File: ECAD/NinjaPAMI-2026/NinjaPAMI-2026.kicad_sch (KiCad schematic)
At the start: 76 parts, among them J1 Con_Batt, J10 CON_EV_01, J11 Conn_01x04, J12 OLED, J13 RightMotor, J14 LeftMotor, J2 Servo, J3 Servo, J4 Sensor_RIGHT, J5 Sensor_Center, J6 Sensor_LEFT, J7 CON_EV_02, J8 CON_EV_02, J9 CON_PUMP_01, Q1 AO3400A, Q2 AO3400A, Q3 AO3400A, Q4 AO3400A, SW1 SW_SPDT, SW2 SW_Reed, SW3 SW_SPDT, U1 R-78E5.0-1.0, U2 XIAO-HALF-HOLE-23P, U3 TMC2209_SILENTSTEPSTICK, U4 TMC2209_SILENTSTEPSTICK

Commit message: placement pump and ev
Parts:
- J12: footprint Connector_PinSocket_2.54mm:PinSocket_1x04_P2.54mm_Vertical -> Connector_Molex:Molex_KK-254_AE-6410-04A_1x04_P2.54mm_Vertical
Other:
- moved on the sheet: D10, D11, D12, D13, D14, D3, D4, D6, D7, J10, J11, J7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

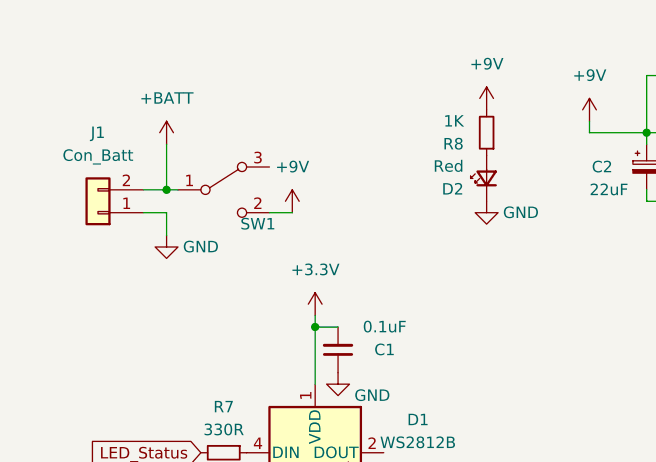
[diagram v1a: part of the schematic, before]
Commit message: modify ARU
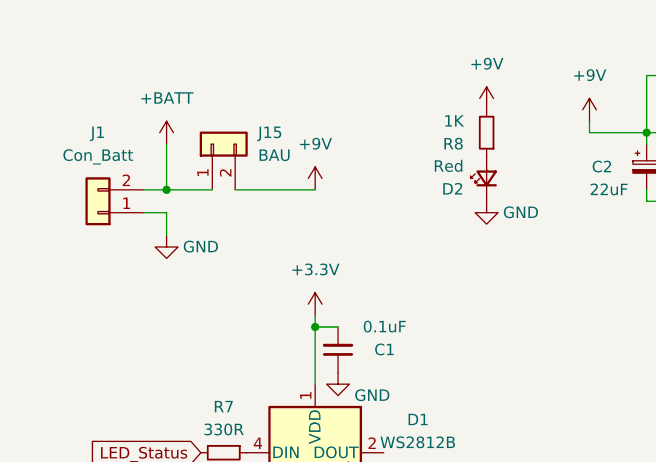
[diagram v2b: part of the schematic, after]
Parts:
- removed SW1: SW_SPDT, PAMI-2025:UB16SKW03N-C, symbol Switch:SW_SPDT
- added J15: BAU, Connector_Molex:Molex_KK-396_A-41791-0002_1x02_P3.96mm_Vertical, symbol Connector_Generic:Conn_01x02
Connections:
- net +9V: now also J15.2 (Pin_2)
- net +BATT: now also J15.1 (Pin_1)
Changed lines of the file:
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@@
 	(wire
 		(pts
-			(xy 25.4 33.02) (xy 26.67 33.02)
+			(xy 25.4 33.02) (xy 30.48 33.02)
 		)
 		(stroke
@@
 	(wire
 		(pts
-			(xy 39.37 35.56) (xy 36.83 35.56)
+			(xy 41.91 33.02) (xy 33.02 33.02)
 		)
 		(stroke
@@
 	)
 	(symbol
+		(lib_id "Connector_Generic:Conn_01x02")
+		(at 30.48 27.94 90)
+		(unit 1)
+		(exclude_from_sim no)
+		(in_bom yes)
+		(on_board yes)
+		(dnp no)
+		(fields_autoplaced yes)
+		(property "Reference" "J15"
+			(at 35.56 26.6699 90)
+			(effects
+				(font
+					(size 1.27 1.27)
+				)
+				(justify right)
+			)
+		)
+		(property "Value" "BAU"
+			(at 35.56 29.2099 90)
+			(effects
+				(font
+					(size 1.27 1.27)
+				)
+				(justify right)
+			)
+		)
+		(property "Footprint" "Connector_Molex:Molex_KK-396_A-41791-0002_1x02_P3.96mm_Vertical"
+			(at 30.48 27.94 0)
+			(effects
+				(font
+					(size 1.27 1.27)
+				)
+				(hide yes)
+			)
+		)
+		(property "Datasheet" "~"
+			(at 30.48 27.94 0)
+			(effects
+				(font
+					(size 1.27 1.27)
+				)
+				(hide yes)
+			)
+		)
+		(property "Description" "Generic connector, single row, 01x02, script generated (kicad-library-utils/schlib/autogen/connector/)"
+			(at 30.48 27.94 0)
+			(effects
+				(font
+					(size 1.27 1.27)
+				)
+				(hide yes)
+			)
+		)
+		(pin "2"
+		)
+		(pin "1"
+		)
+		(instances
+			(project ""
+				(path "/d3e1aeb6-1412-4438-ac7d-372534bf2609"
+					(reference "J15")
+					(unit 1)
+				)
+			)
+		)
+	)
+	(symbol
 		(lib_id "Device:R_Small")
 		(at 25.4 90.17 270)
@@
 	)
 	(symbol
-		(lib_name "SW_SPDT_1")
-		(lib_id "Switch:SW_SPDT")
-		(at 31.75 33.02 0)
-		(unit 1)
-		(exclude_from_sim no)
-		(in_bom yes)
-		(on_board yes)
-		(dnp no)
-		(property "Reference" "SW1"
-			(at 35.56 36.83 0)
-			(effects
-				(font
-					(size 1.27 1.27)
-				)
-			)
-		)
-		(property "Value" "SW_SPDT"
-			(at 45.72 34.29 0)
-			(effects
-				(font
-					(size 1.27 1.27)
-				)
-				(hide yes)
-			)
-		)
-		(property "Footprint" "PAMI-2025:UB16SKW03N-C"
-			(at 31.75 33.02 0)
-			(effects
-				(font
-					(size 1.27 1.27)
-				)
-				(hide yes)
-			)
-		)
-		(property "Datasheet" "https://www.mouser.fr/datasheet/2/295/ubnonilluminated-1507076.pdf"
-			(at 31.75 33.02 0)
-			(effects
-				(font
-					(size 1.27 1.27)
-				)
-				(hide yes)
-			)
-		)
-		(property "Description" ""
-			(at 31.75 33.02 0)
-			(effects
-				(font
-					(size 1.27 1.27)
-				)
-				(hide yes)
-			)
-		)
-		(pin "1"
-		)
-		(pin "2"
-		)
-		(pin "3"
-		)
-		(instances
-			(project "MainBoard-PAMI-2025"
-				(path "/d3e1aeb6-1412-4438-ac7d-372534bf2609"
-					(reference "SW1")
-					(unit 1)
-				)
-			)
-		)
-	)
-	(symbol
 		(lib_id "power:+9V")
 		(at 60.96 24.13 0)
@@
 	(symbol
 		(lib_id "power:+9V")
-		(at 39.37 35.56 0)
+		(at 41.91 33.02 0)
 		(unit 1)
 		(exclude_from_sim no)
@@
 		(fields_autoplaced yes)
 		(property "Reference" "#PWR015"
-			(at 39.37 39.37 0)
+			(at 41.91 36.83 0)
 			(effects
 				(font
@@
 		)
 		(property "Value" "+9V"
-			(at 39.37 30.48 0)
+			(at 41.91 27.94 0)
 			(effects
 				(font
@@
 		)
 		(property "Footprint" ""
-			(at 39.37 35.56 0)
+			(at 41.91 33.02 0)
 			(effects
 				(font
@@
 		)
 		(property "Datasheet" ""
-			(at 39.37 35.56 0)
+			(at 41.91 33.02 0)
 			(effects
 				(font
@@
 		)
 		(property "Description" "Power symbol creates a global label with name \"+9V\""
-			(at 39.37 35.56 0)
+			(at 41.91 33.02 0)
 			(effects
 				(font

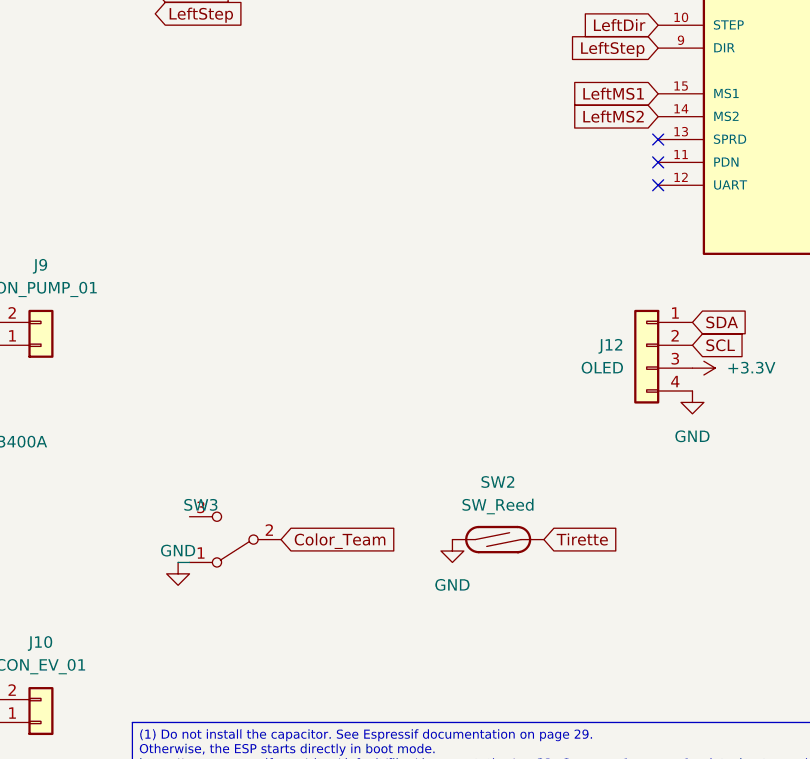
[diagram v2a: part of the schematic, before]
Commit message: add hall effect sensor
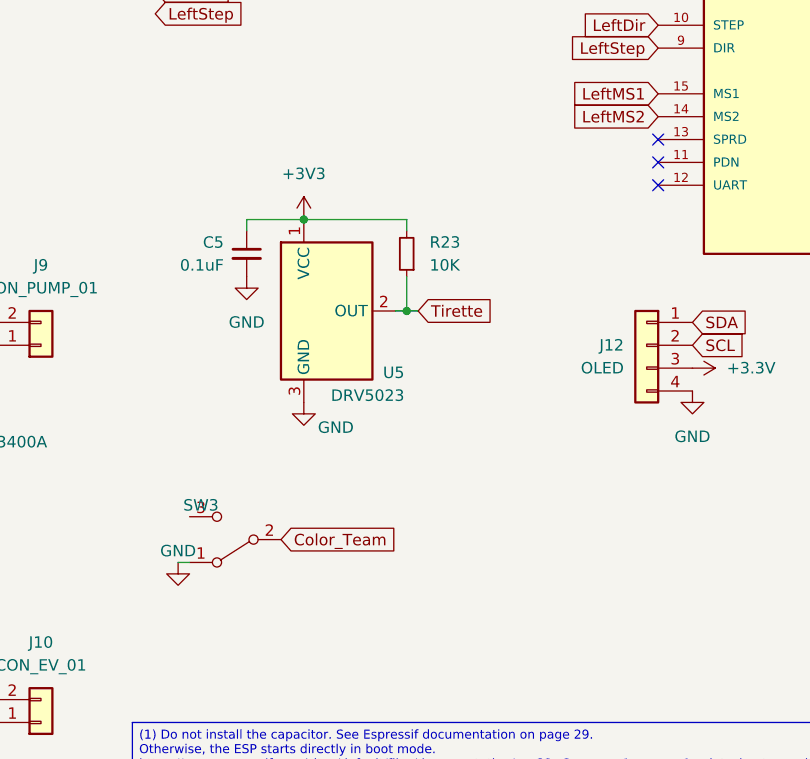
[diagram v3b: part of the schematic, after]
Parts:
- removed SW2: SW_Reed, Button_Switch_SMD:SW_SPST_REED_CT05-XXXX-G1, symbol Switch:SW_Reed
- added C5: 0.1uF, Capacitor_SMD:C_1206_3216Metric_Pad1.33x1.80mm_HandSolder, symbol Device:C_Small
- added R23: 10K, Resistor_SMD:R_1206_3216Metric_Pad1.30x1.75mm_HandSolder, symbol Device:R_Small
- added U5: DRV5023, Package_TO_SOT_SMD:SOT-23_Handsoldering, symbol Sensor_Magnetic:DRV5033AJxDBZ
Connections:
- net GND: now also C5.2, U5.3 (GND)
- net Tirette: now also R23.1, U5.2 (OUT)
- new net +3V3: C5.1, R23.2, U5.1 (VCC)

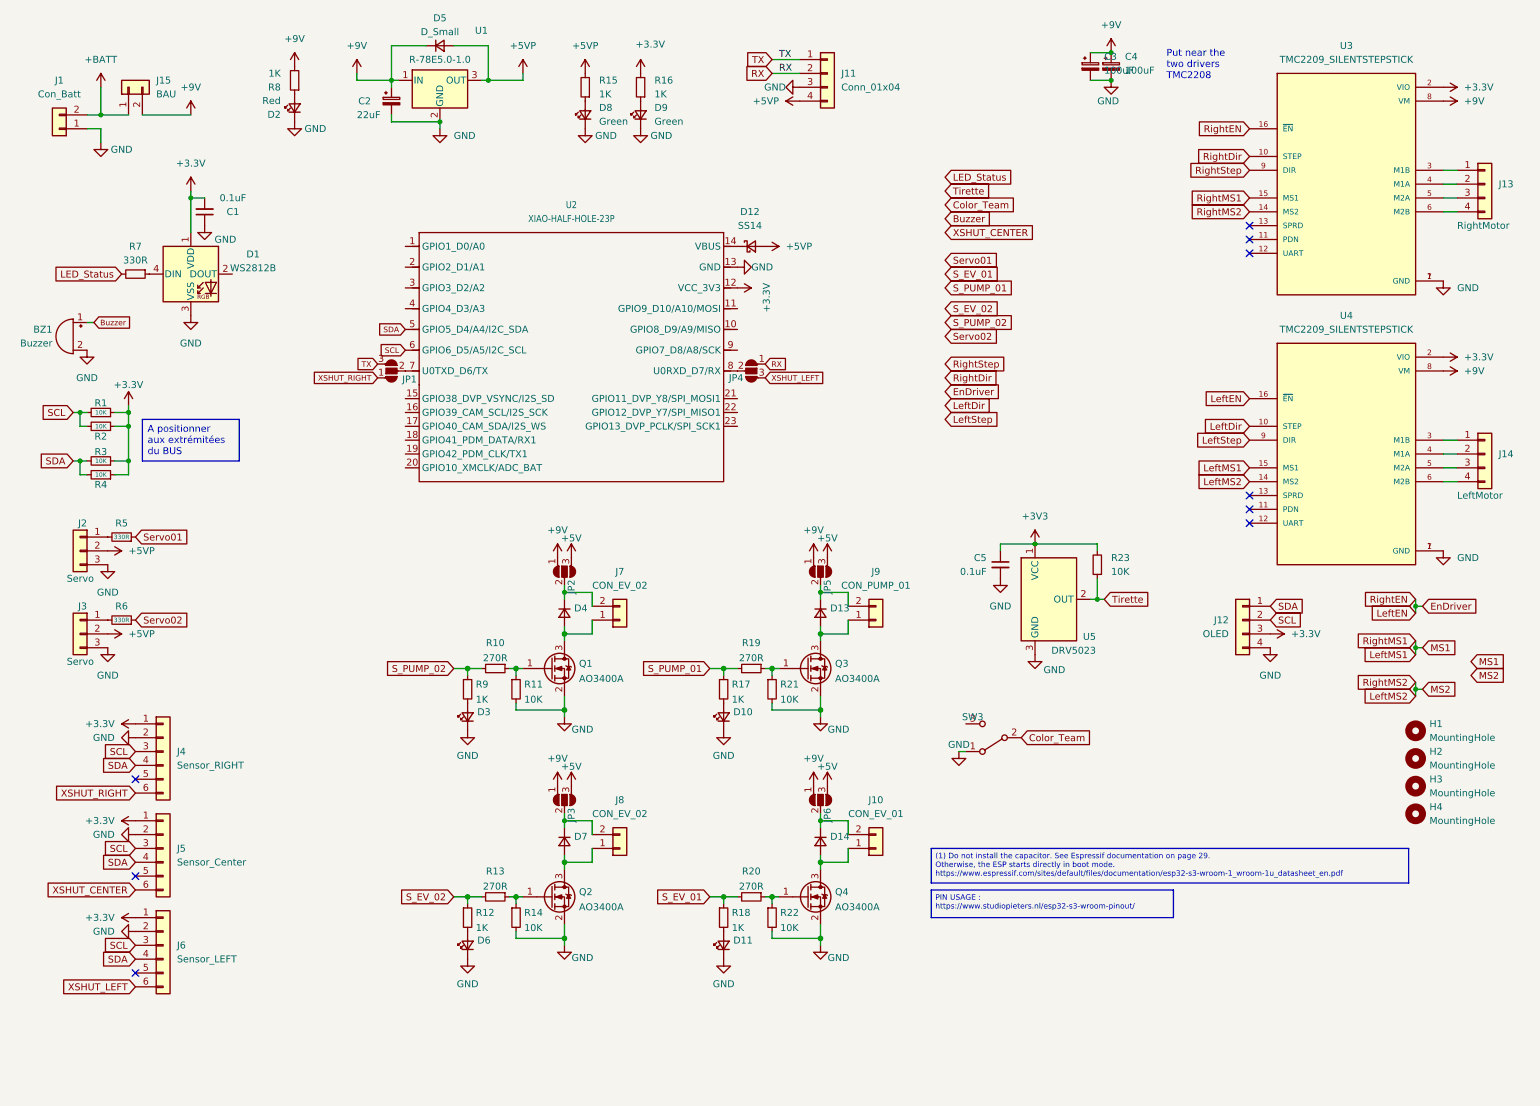
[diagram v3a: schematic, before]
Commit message: size refactor - add 2.0 regulator
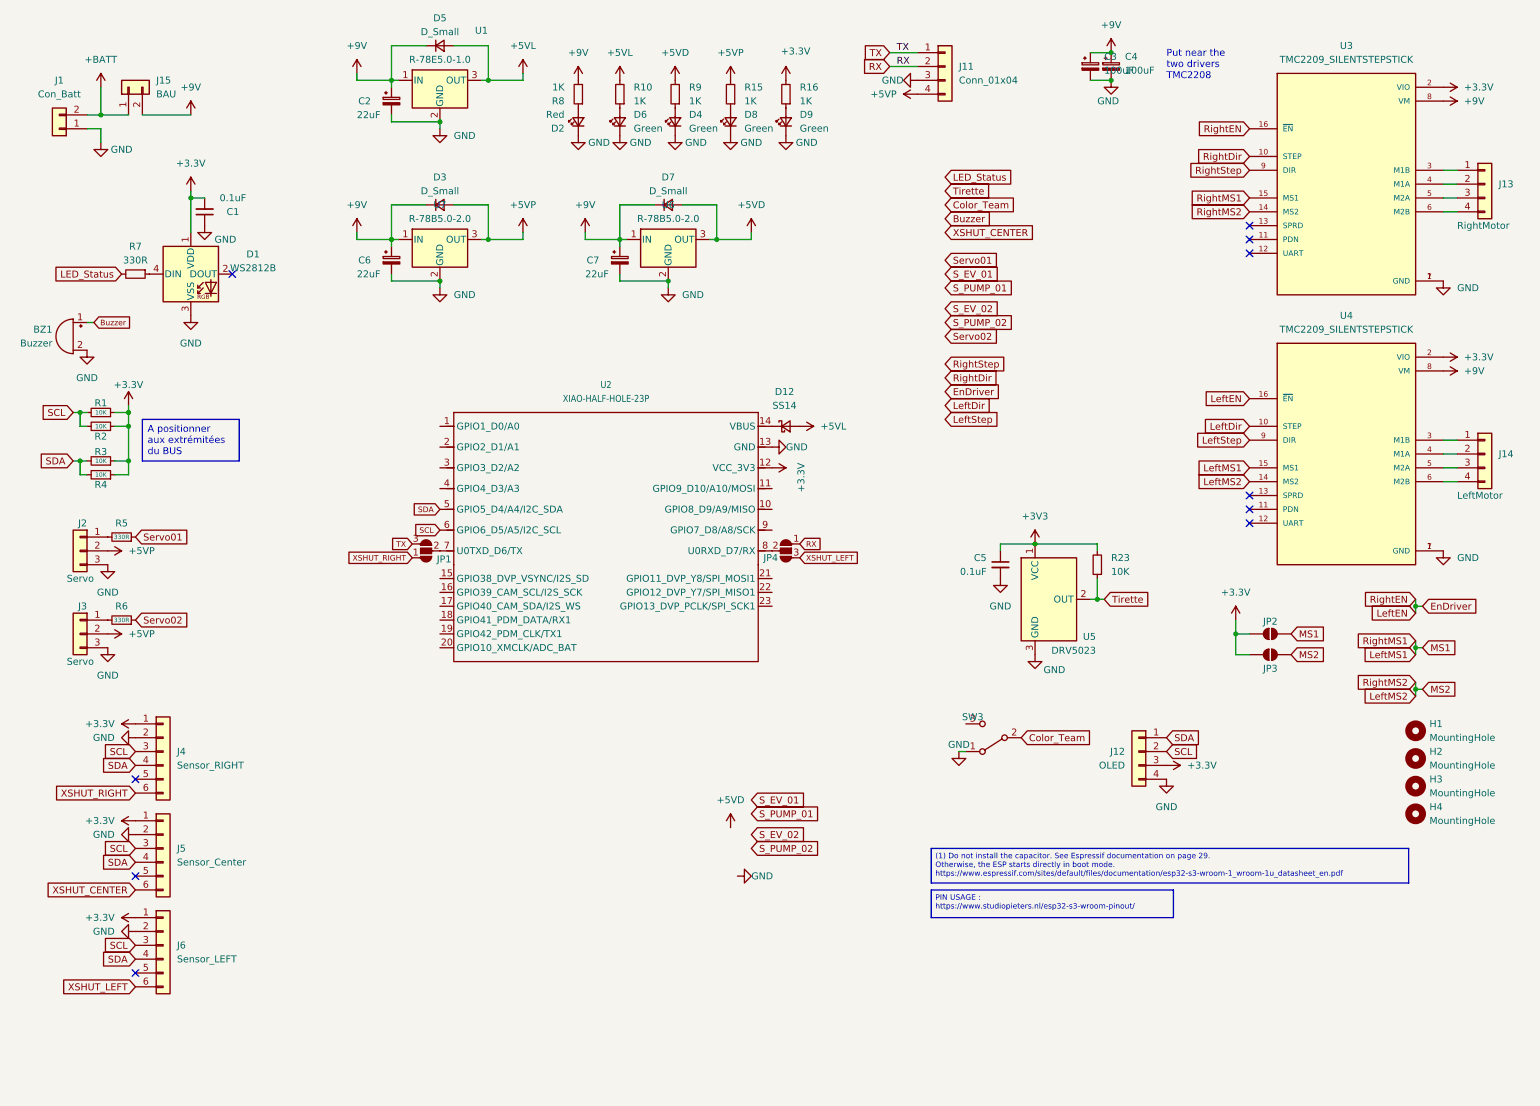
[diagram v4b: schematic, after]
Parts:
- removed D10, D11, D3: LED_Small, LED_SMD:LED_1206_3216Metric_Pad1.42x1.75mm_HandSolder, symbol Device:LED_Small
- removed D13, D14, D4: D_Small, Diode_SMD:D_SMA_Handsoldering, symbol Device:D_Small
- removed J10: CON_EV_01, Connector_Molex:Molex_KK-254_AE-6410-02A_1x02_P2.54mm_Vertical, symbol Connector_Generic:Conn_01x02
- removed J7, J8: CON_EV_02, Connector_Molex:Molex_KK-254_AE-6410-02A_1x02_P2.54mm_Vertical, symbol Connector_Generic:Conn_01x02
- removed J9: CON_PUMP_01, Connector_Molex:Molex_KK-254_AE-6410-02A_1x02_P2.54mm_Vertical, symbol Connector_Generic:Conn_01x02
- removed JP2, JP3, JP5, JP6: SolderJumper_3_Open, Jumper:SolderJumper-3_P1.3mm_Open_RoundedPad1.0x1.5mm_NumberLabels, symbol Jumper:SolderJumper_3_Open
- removed Q1, Q2, Q3, Q4: AO3400A, Package_TO_SOT_SMD:SOT-23, symbol Transistor_FET:AO3400A
- removed R11, R14, R21, R22: 10K, Resistor_SMD:R_1206_3216Metric_Pad1.30x1.75mm_HandSolder, symbol Device:R_Small
- removed R12, R17, R18: 1K, Resistor_SMD:R_1206_3216Metric_Pad1.30x1.75mm_HandSolder, symbol Device:R_Small
- removed R13, R19, R20: 270R, Resistor_SMD:R_1206_3216Metric_Pad1.30x1.75mm_HandSolder, symbol Device:R_Small
- added C6, C7: 22uF, Capacitor_SMD:CP_Elec_5x5.4, symbol Device:CP_Small
- added D3: D_Small, Diode_SMD:D_SMA_Handsoldering, symbol Device:D_Small
- added D4: Green, LED_SMD:LED_1206_3216Metric, symbol Device:LED_Small
- added JP2, JP3: SolderJumper_2_Open, Jumper:SolderJumper-2_P1.3mm_Open_RoundedPad1.0x1.5mm, symbol Jumper:SolderJumper_2_Open
- added U6, U7: R-78B5.0-2.0, Converter_DCDC:Converter_DCDC_RECOM_R-78B-2.0_THT, symbol Converter_DCDC:R-78B5.0-2.0
- D6: value LED_Small -> Green; footprint LED_SMD:LED_1206_3216Metric_Pad1.42x1.75mm_HandSolder -> LED_SMD:LED_1206_3216Metric
- R10: value 270R -> 1K
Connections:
- net +3.3V: now also JP2.1 (A), JP3.1 (A)
- net +5VP: now also D3.2 (A), U7.3 (OUT); no longer D12.2 (A), D5.2 (A), U1.3 (OUT)
- net +9V: now also D7.1 (K), C6.1, C7.1, D3.1 (K), U6.1 (IN), U7.1 (IN)
- net GND: now also C6.2, C7.2, D4.1 (K), U6.2 (GND), U7.2 (GND)
- net LeftMS1: now also JP2.2 (B)
- net LeftMS2: now also JP3.2 (B)
- net S_PUMP_02: no longer R10.2, R9.1
- net at R10.1: now also D6.2 (A)
- net +5VD: now reaches D7.2 (A)
- net +5VD: now also R9.2, U6.3 (OUT)
- new net: D4.2 (A), R9.1
- new net +5VL: D12.2 (A), D5.2 (A), R10.2, U1.3 (OUT)
- no-connect marks 9 -> 10
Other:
- moved on the sheet: D12, D2, D8, D9, J11, J12, JP1, JP4, R15, R16, R8, U2

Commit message: routing and silkscreen
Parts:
- added J7, J8: Conn_01x04, Connector_Molex:Molex_KK-254_AE-6410-04A_1x04_P2.54mm_Vertical, symbol Connector_Generic:Conn_01x04
- added JP5, JP6: SolderJumper_2_Open, Jumper:SolderJumper-2_P1.3mm_Open_RoundedPad1.0x1.5mm, symbol Jumper:SolderJumper_2_Open
- J15: footprint Connector_Molex:Molex_KK-396_A-41791-0002_1x02_P3.96mm_Vertical -> Connector_Molex:Molex_KK-254_AE-6410-02A_1x02_P2.54mm_Vertical
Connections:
- net +3V3 is gone; now on net +3.3V: C5.1, R23.2, U5.1 (VCC)
- net +3.3V: now also J12.1 (Pin_1), JP5.1 (A), JP6.1 (A); no longer J12.3 (Pin_3)
- net +5VD: now also J11.4 (Pin_4), J2.2 (Pin_2), J3.2 (Pin_2)
- net +5VP: now also J7.3 (Pin_3), J8.3 (Pin_3); no longer J11.4 (Pin_4), J2.2 (Pin_2), J3.2 (Pin_2)
- net Buzzer: now also U2.1 (GPIO1_D0/A0)
- net Color_Team: now also U2.16 (GPIO39_CAM_SCL/I2S_SCK)
- net EnDriver: now also U2.4 (GPIO4_D3/A3)
- net GND: now also J12.2 (Pin_2), J7.4 (Pin_4), J8.4 (Pin_4); no longer J12.4 (Pin_4)
- net LED_Status: now also U2.2 (GPIO2_D1/A1)
- net LeftDir: now also U2.17 (GPIO40_CAM_SDA/I2S_WS)
- net LeftMS1: now also JP5.2 (B); no longer JP2.2 (B), U3.15 (MS1)
- net LeftMS2: now also JP6.2 (B); no longer JP3.2 (B), U3.14 (MS2)
- net LeftStep: now also U2.3 (GPIO3_D2/A2)
- net RightDir: now also U2.18 (GPIO41_PDM_DATA/RX1)
- net RightStep: now also U2.19 (GPIO42_PDM_CLK/TX1)
- net SCL: now also J12.3 (Pin_3); no longer J12.2 (Pin_2)
- net SDA: now also J12.4 (Pin_4); no longer J12.1 (Pin_1)
- net S_EV_01: now also U2.9 (GPIO7_D8/A8/SCK), J7.2 (Pin_2)
- net S_EV_02: now also U2.22 (GPIO12_DVP_Y7/SPI_MISO1), J8.2 (Pin_2)
- net S_PUMP_01: now also U2.21 (GPIO11_DVP_Y8/SPI_MOSI1), J7.1 (Pin_1)
- net S_PUMP_02: now also U2.10 (GPIO8_D9/A9/MISO), J8.1 (Pin_1)
- net Servo01: now also U2.23 (GPIO13_DVP_PCLK/SPI_SCK1)
- net Servo02: now also U2.11 (GPIO9_D10/A10/MOSI)
- net Tirette: now also U2.15 (GPIO38_DVP_VSYNC/I2S_SD)
- net XSHUT_CENTER: now also U2.20 (GPIO10_XMCLK/ADC_BAT)
- new net RightMS1: JP2.2 (B), U3.15 (MS1)
- new net RightMS2: JP3.2 (B), U3.14 (MS2)
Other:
- moved on the sheet: J12, JP2, JP3
